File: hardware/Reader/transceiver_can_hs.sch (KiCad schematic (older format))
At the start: 0 parts

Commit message: Completed schematics for reader
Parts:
- added C_HSCAN_1, C_HSCAN_2: 560pF, footprints:CAPC1608X90, symbol Device:C
- added C_HSCAN_3: 1uF, footprints:0603, symbol Device:C
- added IC3: MCP2562-H_MF, footprints:MCP2562-H&slash_MF, symbol MCP2562HMF:MCP2562-H_MF
- added Q_HSCAN_1: NX7002AK,215, footprints:SOT95P230X110-3N, symbol NX7002AK_215:NX7002AK,215
- added Q_HSCAN_2: PESD2CAN,215, footprints:SOT95P230X110-3N, symbol PESD2CAN_215:PESD2CAN,215
- added R_HSCAN_1: 100k, footprints:RESC1608X55N, symbol Device:R_Small
- added R_HSCAN_2, R_HSCAN_3: 100, footprints:RESC3216X70N, symbol Device:R_Small
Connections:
- new net: IC3.8 (STBY), Q_HSCAN_1.3, R_HSCAN_1.2
- new net: C_HSCAN_1.1, R_HSCAN_2.2
- new net: C_HSCAN_2.1, R_HSCAN_3.2
- new net +3V3: IC3.5 (VIO), R_HSCAN_1.1
- new net +5V: C_HSCAN_3.2, IC3.3 (VDD)
- new net GND: C_HSCAN_1.2, C_HSCAN_2.2, C_HSCAN_3.1, IC3.2 (VSS), IC3.9 (EPAD), Q_HSCAN_1.2, Q_HSCAN_2.3
- new net HS_CAN_High: IC3.7 (CANH), Q_HSCAN_2.1, R_HSCAN_3.1
- new net HS_CAN_Low: IC3.6 (CANL), Q_HSCAN_2.2, R_HSCAN_2.1
- new net HS_CAN_RX: IC3.4 (RXD)
- new net HS_CAN_TX: IC3.1 (TXD)
- new net ~PWR_CTRL~: Q_HSCAN_1.1
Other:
- note added: "ESD Protection"

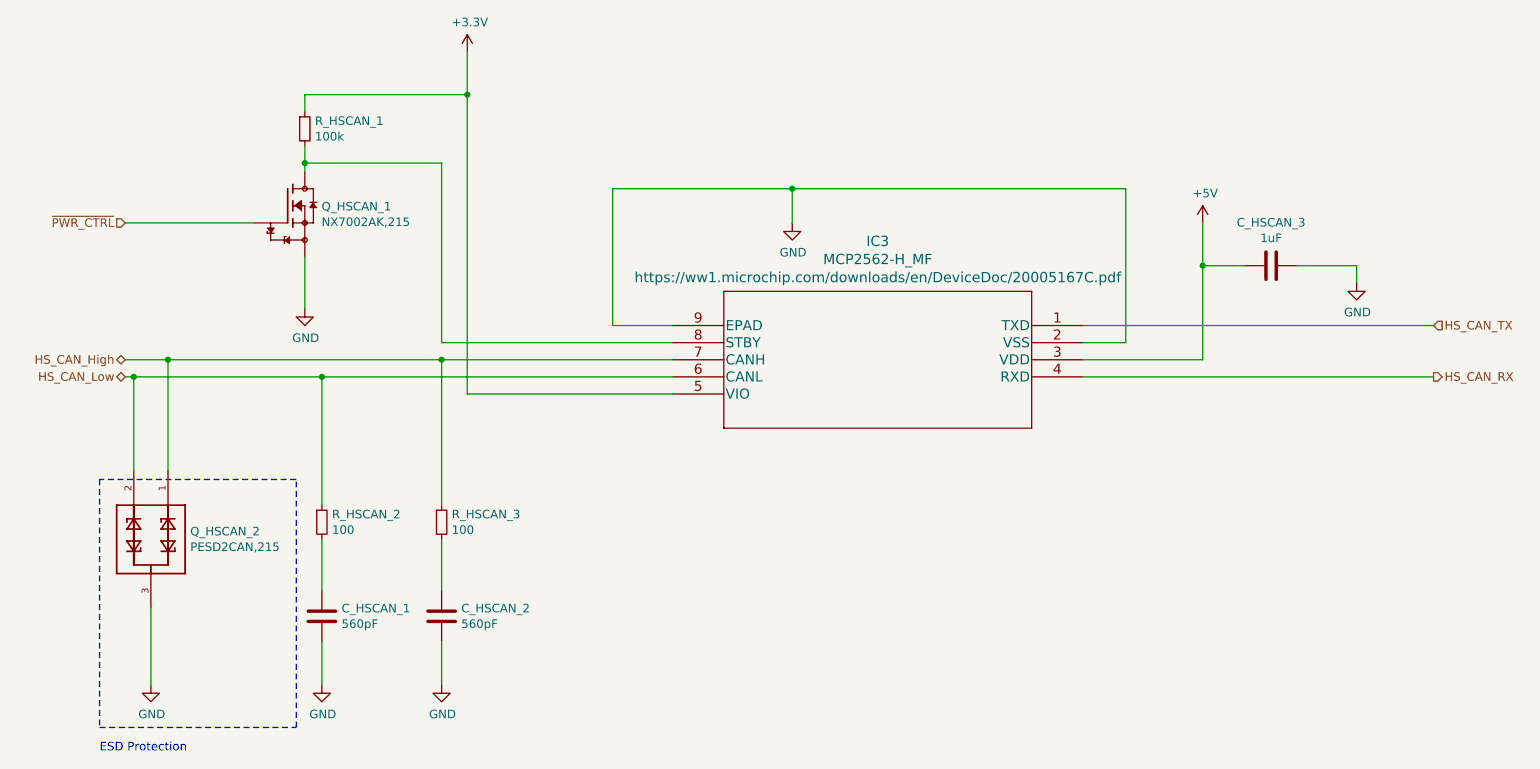
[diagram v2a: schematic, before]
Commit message: Added ESD Protection. Fixed minor bugs on schematic. Attempted placement of components
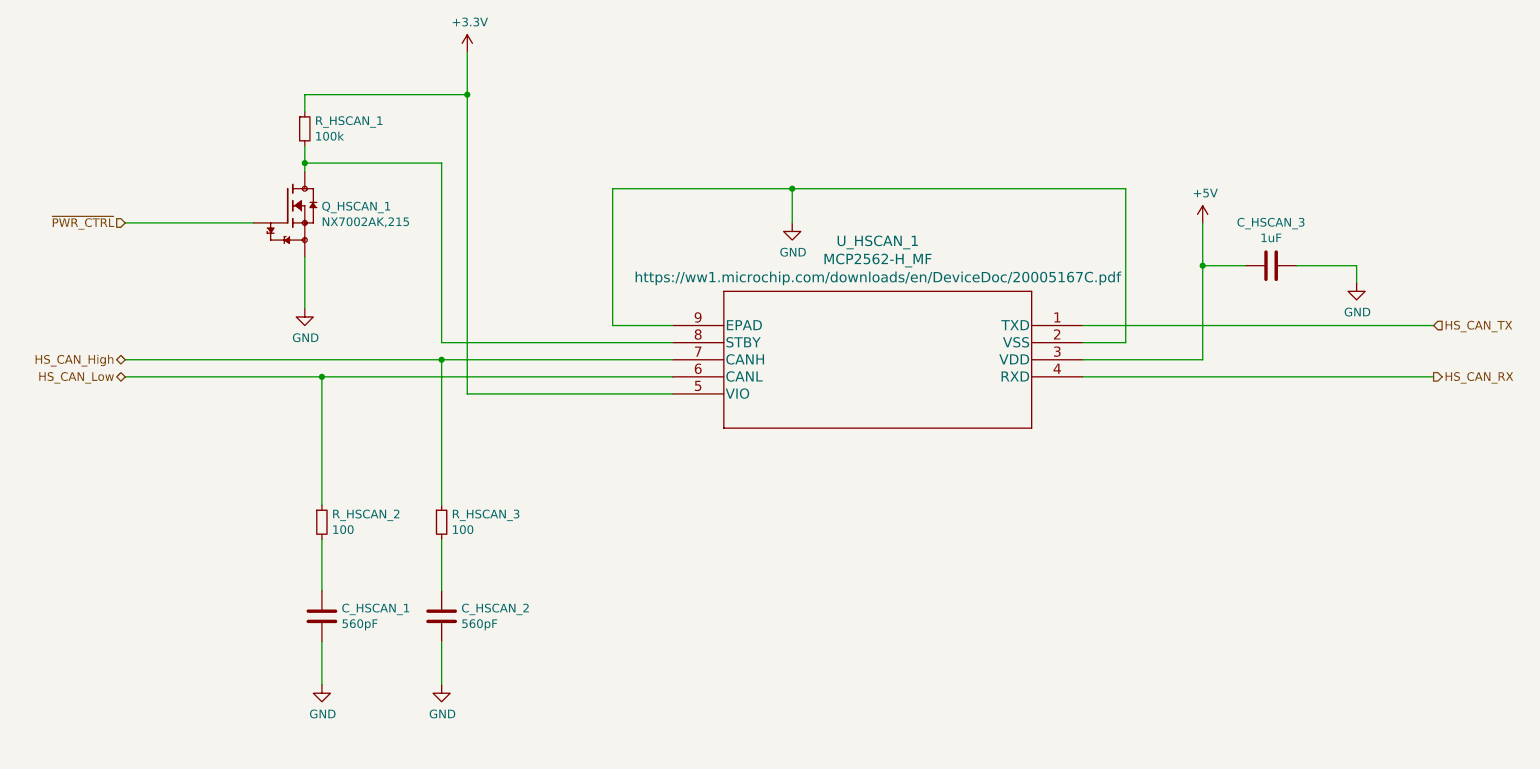
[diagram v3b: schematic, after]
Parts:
- removed Q_HSCAN_2: PESD2CAN,215, footprints:SOT95P230X110-3N, symbol PESD2CAN_215:PESD2CAN,215
- renumbered IC3 to U_HSCAN_1
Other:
- note removed: "ESD Protection"
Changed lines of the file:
@@
 $Descr USLetter 11000 8500
 encoding utf-8
-Sheet 10 18
+Sheet 5 19
 Title "CANnect Reader | High Speed CAN Transceiver"
-Date "2020-10-20"
-Rev "0.0.01"
+Date "2020-10-25"
+Rev "0.0.03"
 Comp "CANtech"
 Comment1 "Created by Choong Jin Ng | jin8383@gmail.com"
@@
 HS_CAN_Low
 $Comp
-L PESD2CAN_215:PESD2CAN,215 Q_HSCAN_2
-U 1 1 5FAF657F
-P 1550 3750
-F 0 "Q_HSCAN_2" V 1504 3980 50  0000 L CNN
-F 1 "PESD2CAN,215" V 1595 3980 50  0000 L CNN
-F 2 "footprints:SOT95P230X110-3N" H 1550 3750 50  0001 L BNN
-F 3 "https://assets.nexperia.com/documents/data-sheet/PESD2CAN.pdf" H 1550 3750 50  0001 L BNN
-	1    1550 3750
-	0    1    1    0
-$EndComp
-Wire Wire Line
-	1400 2700 1650 2700
-$Comp
-L power:GND #PWR0131
-U 1 1 5FAF7C00
-P 1550 4600
-F 0 "#PWR0131" H 1550 4350 50  0001 C CNN
-F 1 "GND" H 1555 4427 50  0000 C CNN
-F 2 "" H 1550 4600 50  0001 C CNN
-F 3 "" H 1550 4600 50  0001 C CNN
-	1    1550 4600
-	1    0    0    -1
-$EndComp
-Wire Wire Line
-	1550 4150 1550 4600
-Wire Notes Line
-	1250 4850 2400 4850
-Wire Notes Line
-	2400 4850 2400 3400
-Wire Notes Line
-	2400 3400 1250 3400
-Wire Notes Line
-	1250 3400 1250 4850
-Text Notes 1250 5000 0    50   ~ 0
-ESD Protection
-$Comp
-L MCP2562HMF:MCP2562-H_MF IC3
+L MCP2562HMF:MCP2562-H_MF U_HSCAN_1
 U 1 1 5FAF8CE0
 P 7000 2500
-F 0 "IC3" H 8200 2993 60  0000 C CNN
+F 0 "U_HSCAN_1" H 8200 2993 60  0000 C CNN
 F 1 "MCP2562-H_MF" H 8200 2887 60  0000 C CNN
 F 2 "footprints:MCP2562-H&slash_MF" H 8200 2740 60  0001 C CNN
@@
 	-1   0    0    -1
 $EndComp
-Wire Wire Line
-	1450 2800 1450 3350
-Connection ~ 1450 2800
-Wire Wire Line
-	1450 2800 1400 2800
-Connection ~ 1650 2700
-Wire Wire Line
-	1650 2700 1650 3350
 $Comp
 L Device:R_Small R_HSCAN_2
@@
 	2550 3550 2550 2800
 Connection ~ 2550 2800
-Wire Wire Line
-	1450 2800 2550 2800
 Wire Wire Line
 	7000 2600 7250 2600
@@
 	5300 1700 4250 1700
 Wire Wire Line
-	1650 2700 3250 2700
-Wire Wire Line
 	3250 3550 3250 2700
 Connection ~ 3250 2700
 Wire Wire Line
 	3250 2700 4600 2700
+Wire Wire Line
+	1400 2800 2550 2800
+Wire Wire Line
+	1400 2700 3250 2700
 $EndSCHEMATC

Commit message: Fixed bugs on the reader schematic. Exported Schematic Electrical report
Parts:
- C_HSCAN_1, C_HSCAN_2: Manufacturer (none) -> Yageo; Part Name (none) -> CC0603KRX7R9BB561; Vendor (none) -> DigiKey Canada; digikeypn (none) -> 311-1079-1-ND
- C_HSCAN_3: Manufacturer (none) -> Kermet; Part Name (none) -> C0603C105K4RACTU; Vendor (none) -> DigiKey Canada; digikeypn (none) -> 399-7847-1-ND
- Q_HSCAN_1: Manufacturer (none) -> Nexperia USA Inc.; Part Name (none) -> NX7002AK,215; Vendor (none) -> DigiKey Canada; digikeypn (none) -> 1727-1289-1-ND
- R_HSCAN_1: Manufacturer (none) -> Yageo; Vendor (none) -> DigiKey Canada; digikeypn (none) -> 311-2395-1-ND
- R_HSCAN_2, R_HSCAN_3: Manufacturer (none) -> Panasonic Electronic Components; Vendor (none) -> DigiKey Canada; digikeypn (none) -> P100FCT-ND
- U_HSCAN_1: Manufacturer (none) -> Microchip Technology; Part Name (none) -> MCP2562-H_MF; Vendor (none) -> DigiKey Canada; digikeypn (none) -> MCP2562-H/MF-ND
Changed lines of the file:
@@
 F 2 "footprints:MCP2562-H&slash_MF" H 8200 2740 60  0001 C CNN
 F 3 "https://ww1.microchip.com/downloads/en/DeviceDoc/20005167C.pdf" H 8200 2781 60  0000 C CNN
+F 4 "MCP2562-H_MF" H 7000 2500 50  0001 C CNN "Part Name"
+F 5 "Microchip Technology" H 7000 2500 50  0001 C CNN "Manufacturer"
+F 6 "DigiKey Canada" H 7000 2500 50  0001 C CNN "Vendor"
+F 7 "MCP2562-H/MF-ND" H 7000 2500 50  0001 C CNN "digikeypn"
 	1    7000 2500
 	-1   0    0    -1
@@
 F 3 "https://industrial.panasonic.com/cdbs/www-data/pdf/RDA0000/AOA0000C304.pdf" H 2550 3650 50  0001 C CNN
 F 4 "ERJ-8ENF1000V" H 2550 3650 50  0001 C CNN "Part Name"
+F 5 "DigiKey Canada" H 2550 3650 50  0001 C CNN "Vendor"
+F 6 "Panasonic Electronic Components" H 2550 3650 50  0001 C CNN "Manufacturer"
+F 7 "P100FCT-ND" H 2550 3650 50  0001 C CNN "digikeypn"
 	1    2550 3650
 	1    0    0    -1
@@
 F 3 "https://industrial.panasonic.com/cdbs/www-data/pdf/RDA0000/AOA0000C304.pdf" H 3250 3650 50  0001 C CNN
 F 4 "ERJ-8ENF1000V" H 3250 3650 50  0001 C CNN "Part Name"
+F 5 "DigiKey Canada" H 3250 3650 50  0001 C CNN "Vendor"
+F 6 "Panasonic Electronic Components" H 3250 3650 50  0001 C CNN "Manufacturer"
+F 7 "P100FCT-ND" H 3250 3650 50  0001 C CNN "digikeypn"
 	1    3250 3650
 	1    0    0    -1
@@
 F 2 "footprints:CAPC1608X90" H 2588 4050 50  0001 C CNN
 F 3 "https://www.yageo.com/upload/media/product/productsearch/datasheet/mlcc/UPY-GPHC_X7R_6.3V-to-50V_18.pdf" H 2550 4200 50  0001 C CNN
+F 4 "CC0603KRX7R9BB561" H 2550 4200 50  0001 C CNN "Part Name"
+F 5 "Yageo" H 2550 4200 50  0001 C CNN "Manufacturer"
+F 6 "DigiKey Canada" H 2550 4200 50  0001 C CNN "Vendor"
+F 7 "311-1079-1-ND" H 2550 4200 50  0001 C CNN "digikeypn"
 	1    2550 4200
 	1    0    0    -1
@@
 F 2 "footprints:CAPC1608X90" H 3288 4050 50  0001 C CNN
 F 3 "https://www.yageo.com/upload/media/product/productsearch/datasheet/mlcc/UPY-GPHC_X7R_6.3V-to-50V_18.pdf" H 3250 4200 50  0001 C CNN
+F 4 "CC0603KRX7R9BB561" H 3250 4200 50  0001 C CNN "Part Name"
+F 5 "Yageo" H 3250 4200 50  0001 C CNN "Manufacturer"
+F 6 "DigiKey Canada" H 3250 4200 50  0001 C CNN "Vendor"
+F 7 "311-1079-1-ND" H 3250 4200 50  0001 C CNN "digikeypn"
 	1    3250 4200
 	1    0    0    -1
@@
 F 5 "7" H 2350 1800 50  0001 L BNN "Field5"
 F 6 "IPC-7351B" H 2350 1800 50  0001 L BNN "Field6"
+F 7 "NX7002AK,215" H 2350 1800 50  0001 C CNN "Part Name"
+F 8 "Nexperia USA Inc." H 2350 1800 50  0001 C CNN "Manufacturer"
+F 9 "DigiKey Canada" H 2350 1800 50  0001 C CNN "Vendor"
+F 10 "1727-1289-1-ND" H 2350 1800 50  0001 C CNN "digikeypn"
 	1    2350 1800
 	1    0    0    -1
@@
 F 3 "https://www.yageo.com/upload/media/product/productsearch/datasheet/rchip/PYu-RT_1-to-0.01_RoHS_L_12.pdf" H 2450 1350 50  0001 C CNN
 F 4 "RT0603DRE07100KL" H 2450 1350 50  0001 C CNN "Part Name"
+F 5 "Yageo" H 2450 1350 50  0001 C CNN "Manufacturer"
+F 6 "DigiKey Canada" H 2450 1350 50  0001 C CNN "Vendor"
+F 7 "311-2395-1-ND" H 2450 1350 50  0001 C CNN "digikeypn"
 	1    2450 1350
 	1    0    0    -1
@@
 F 2 "footprints:0603" H 8138 2000 50  0001 C CNN
 F 3 "https://content.kemet.com/datasheets/KEM_C1002_X7R_SMD.pdf" H 8100 2150 50  0001 C CNN
+F 4 "C0603C105K4RACTU" H 8100 2150 50  0001 C CNN "Part Name"
+F 5 "Kermet" H 8100 2150 50  0001 C CNN "Manufacturer"
+F 6 "DigiKey Canada" H 8100 2150 50  0001 C CNN "Vendor"
+F 7 "399-7847-1-ND" H 8100 2150 50  0001 C CNN "digikeypn"
 	1    8100 2150
 	0    1    1    0
